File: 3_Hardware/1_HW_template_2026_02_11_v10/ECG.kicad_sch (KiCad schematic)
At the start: 25 parts, among them U5 AD8232ACPZ-R7

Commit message: added datasheet and started layout
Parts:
- renumbered LA to LA1, RA to RA1, RL to RL1
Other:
- moved on the sheet: C25, C26, C27, C28, C29, C30, C31, LA1, R23, R24, R25, R28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

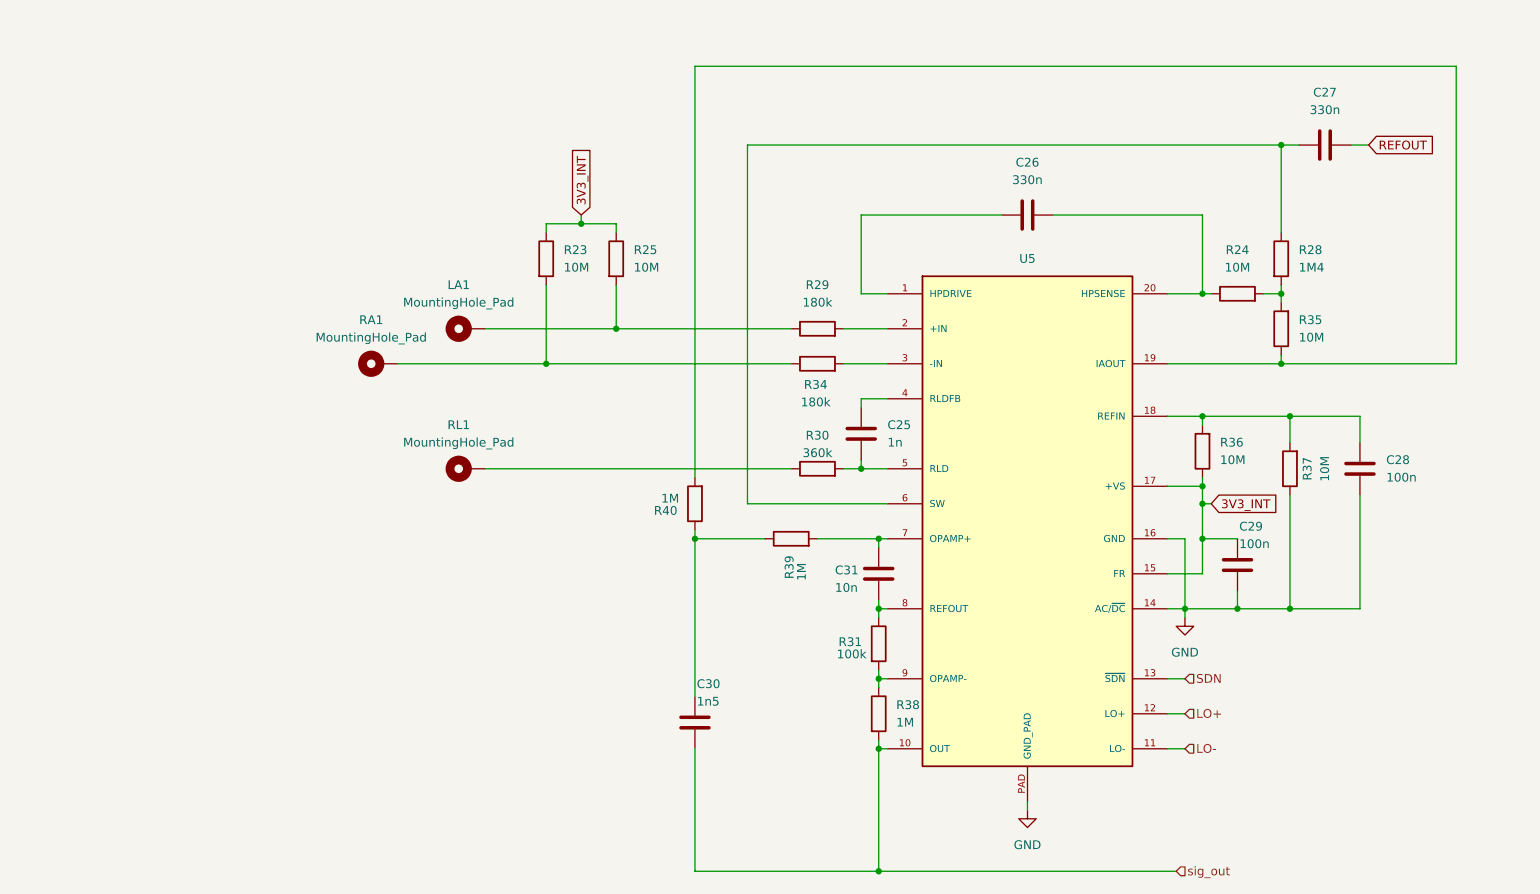
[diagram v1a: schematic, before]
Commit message: updated layout
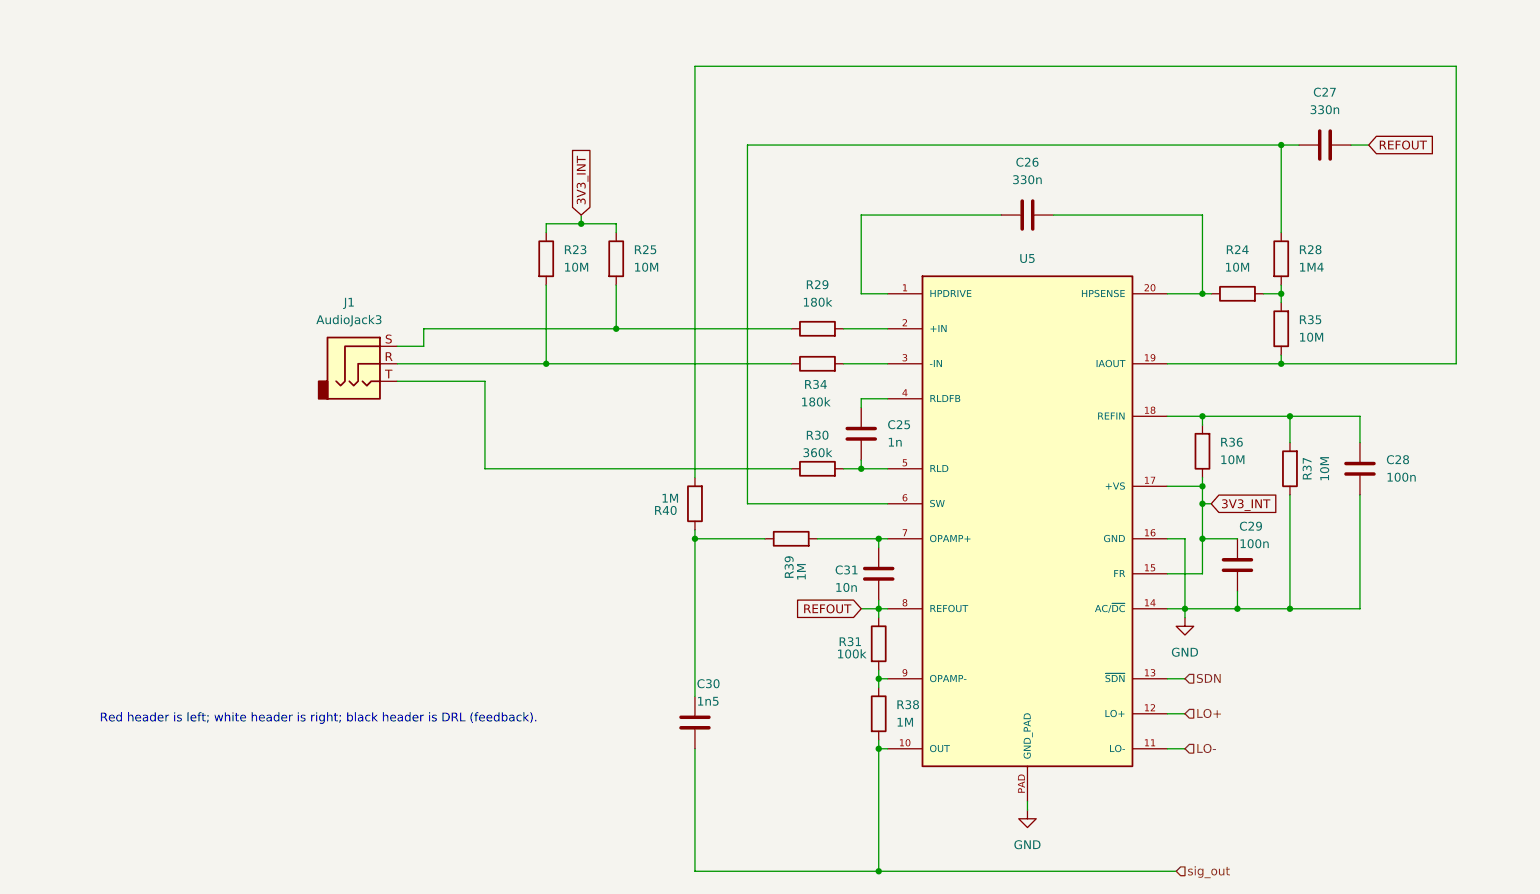
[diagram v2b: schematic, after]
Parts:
- removed LA1, RA1, RL1: MountingHole_Pad, TestPoint:TestPoint_Loop_D2.60mm_Drill1.6mm_Beaded, symbol Mechanical:MountingHole_Pad
- added J1: AudioJack3, Connector_Audio:Jack_3.5mm_CUI_SJ-3523-SMT_Horizontal, symbol Connector_Audio:AudioJack3
- R23, R24, R25, R28, R29, R30, R31, R34, R35, R36, R37, R38, R39, R40: footprint Resistor_SMD:R_0805_2012Metric_Pad1.20x1.40mm_HandSolder -> Resistor_SMD:R_0603_1608Metric_Pad0.98x0.95mm_HandSolder
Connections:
- net REFOUT: now also C31.1, R31.1, U5.8 (REFOUT)
- net at R23.2, R34.1: now also J1.R
- net at R25.2, R29.1: now also J1.S
- net at R30.1: now also J1.T
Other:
- note added: "Red header is left; white header is right; black header is DRL (feedback)."

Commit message: updated layout
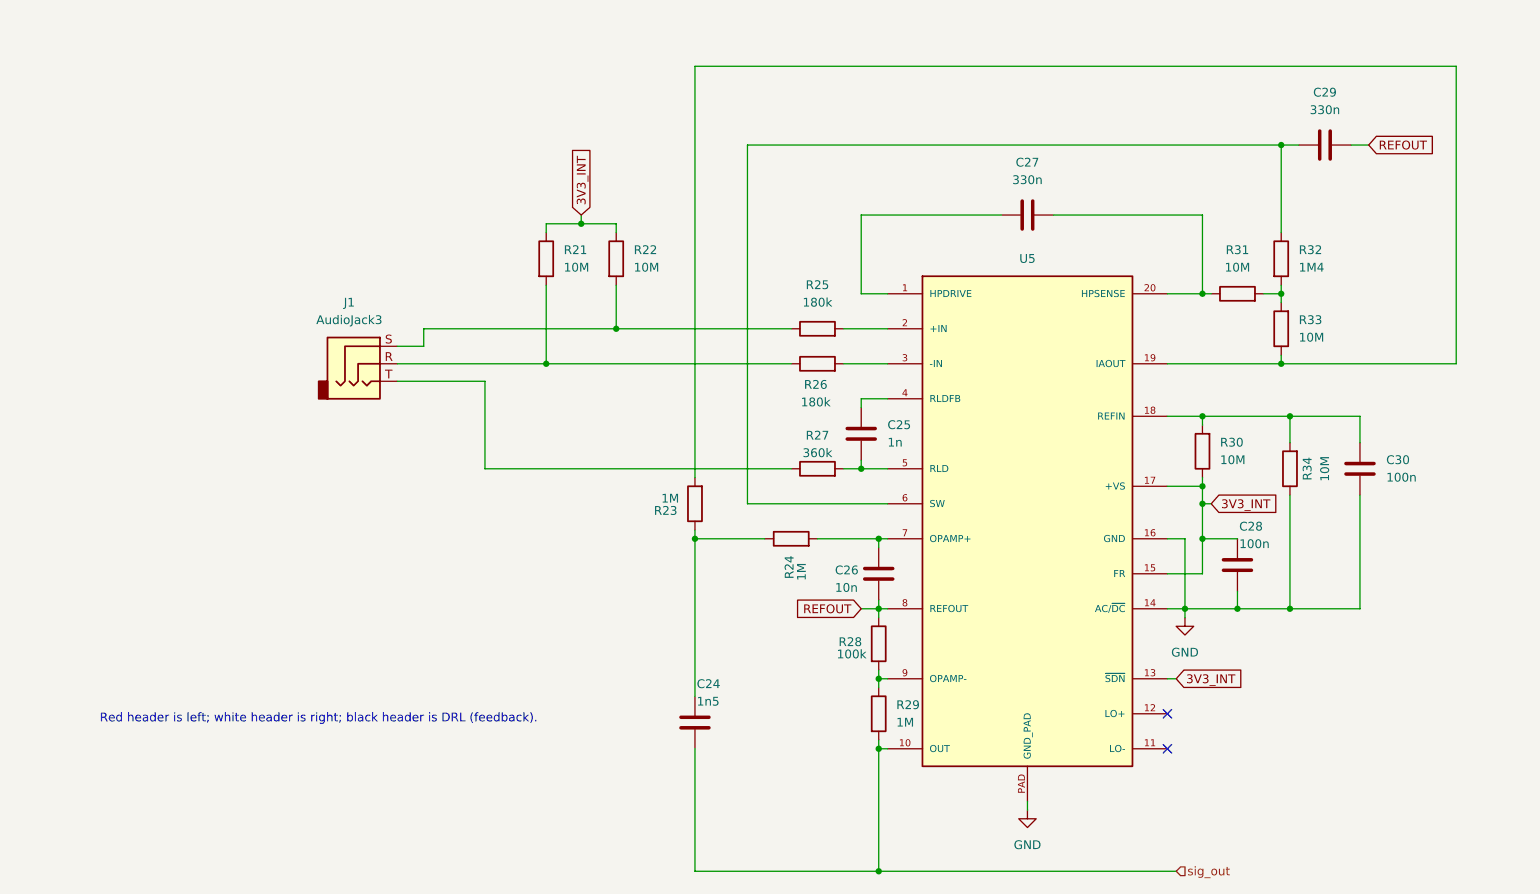
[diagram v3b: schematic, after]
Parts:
- renumbered C30 to C24, C31 to C26, C26 to C27, C29 to C28, C27 to C29, C28 to C30, R23 to R21, R25 to R22, R40 to R23, R39 to R24, R29 to R25, R34 to R26, R30 to R27, R31 to R28, R38 to R29, R36 to R30, R24 to R31, R28 to R32, R35 to R33, R37 to R34
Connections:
- net SDN is gone; now on net 3V3_INT: U5.13 (~{SDN})
- net LO+: no longer names the net of U5.12 (LO+)
- net LO-: no longer names the net of U5.11 (LO-)
- no-connect marks 0 -> 2
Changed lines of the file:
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@@
 		(color 0 0 0 0)
 	)
+	(no_connect
+		(at 175.26 128.27)
+	)
+	(no_connect
+		(at 175.26 123.19)
+	)
 	(wire
 		(pts
@@
 	(wire
 		(pts
+			(xy 176.53 118.11) (xy 175.26 118.11)
+		)
+		(stroke
+			(width 0)
+			(type default)
+		)
+	)
+	(wire
+		(pts
 			(xy 133.35 97.79) (xy 134.62 97.79)
 		)
@@
 	(wire
 		(pts
-			(xy 175.26 123.19) (xy 177.8 123.19)
-		)
-		(stroke
-			(width 0)
-			(type default)
-		)
-	)
-	(wire
-		(pts
 			(xy 193.04 80.01) (xy 193.04 83.82)
 		)
@@
 	(wire
 		(pts
-			(xy 175.26 128.27) (xy 177.8 128.27)
-		)
-		(stroke
-			(width 0)
-			(type default)
-		)
-	)
-	(wire
-		(pts
 			(xy 180.34 50.8) (xy 180.34 62.23)
 		)
@@
 	(wire
 		(pts
-			(xy 175.26 118.11) (xy 177.8 118.11)
-		)
-		(stroke
-			(width 0)
-			(type default)
-		)
-	)
-	(wire
-		(pts
 			(xy 106.68 96.52) (xy 106.68 97.79)
 		)
@@
 		)
 	)
-	(global_label "REFOUT"
+	(global_label "3V3_INT"
 		(shape input)
-		(at 130.81 107.95 180)
+		(at 176.53 118.11 0)
 		(fields_autoplaced yes)
 		(effects
@@
 				(size 1.27 1.27)
 			)
-			(justify right)
+			(justify left)
 		)
 		(property "Intersheetrefs" "${INTERSHEET_REFS}"
-			(at 120.6886 107.95 0)
+			(at 186.8933 118.11 0)
 			(effects
 				(font
 					(size 1.27 1.27)
 				)
-				(justify right)
+				(justify left)
 				(hide yes)
 			)
 		)
 	)
-	(hierarchical_label "LO-"
-		(shape input)
-		(at 177.8 128.27 0)
-		(effects
-			(font
-				(size 1.27 1.27)
-			)
-			(justify left)
-		)
-	)
-	(hierarchical_label "sig_out"
+	(global_label "REFOUT"
 		(shape input)
-		(at 176.53 146.05 0)
+		(at 130.81 107.95 180)
+		(fields_autoplaced yes)
 		(effects
 			(font
 				(size 1.27 1.27)
 			)
-			(justify left)
+			(justify right)
 		)
-	)
-	(hierarchical_label "LO+"
-		(shape input)
-		(at 177.8 123.19 0)
-		(effects
-			(font
-				(size 1.27 1.27)
+		(property "Intersheetrefs" "${INTERSHEET_REFS}"
+			(at 120.6886 107.95 0)
+			(effects
+				(font
+					(size 1.27 1.27)
+				)
+				(justify right)
+				(hide yes)
 			)
-			(justify left)
 		)
 	)
-	(hierarchical_label "SDN"
+	(hierarchical_label "sig_out"
 		(shape input)
-		(at 177.8 118.11 0)
+		(at 176.53 146.05 0)
 		(effects
 			(font
@@
 		(on_board yes)
 		(dnp no)
-		(property "Reference" "R34"
+		(property "Reference" "R26"
 			(at 124.206 75.438 90)
 			(effects
@@
 			(project "HW_template"
 				(path "/1f276d59-ad9b-4e70-a842-f3b7e562eb9b/0fb14f5e-532a-4fc6-a21e-2193a42ea5a4"
-					(reference "R34")
+					(reference "R26")
 					(unit 1)
 				)
@@
 		(dnp no)
 		(fields_autoplaced yes)
-		(property "Reference" "R36"
+		(property "Reference" "R30"
 			(at 182.88 83.8199 0)
 			(effects
@@
 			(project "HW_template"
 				(path "/1f276d59-ad9b-4e70-a842-f3b7e562eb9b/0fb14f5e-532a-4fc6-a21e-2193a42ea5a4"
-					(reference "R36")
+					(reference "R30")
 					(unit 1)
 				)
@@
 		(dnp no)
 		(fields_autoplaced yes)
-		(property "Reference" "#PWR041"
+		(property "Reference" "#PWR040"
 			(at 177.8 115.57 0)
 			(effects
@@
 			(project "HW_template"
 				(path "/1f276d59-ad9b-4e70-a842-f3b7e562eb9b/0fb14f5e-532a-4fc6-a21e-2193a42ea5a4"
-					(reference "#PWR041")
+					(reference "#PWR040")
 					(unit 1)
 				)
@@
 		(dnp no)
 		(fields_autoplaced yes)
-		(property "Reference" "R35"
+		(property "Reference" "R33"
 			(at 194.31 66.0399 0)
 			(effects
@@
 			(project "HW_template"
 				(path "/1f276d59-ad9b-4e70-a842-f3b7e562eb9b/0fb14f5e-532a-4fc6-a21e-2193a42ea5a4"
-					(reference "R35")
+					(reference "R33")
 					(unit 1)
 				)
@@
 		(on_board yes)
 		(dnp no)
-		(property "Reference" "R40"
+		(property "Reference" "R23"
 			(at 104.14 93.726 0)
 			(effects
@@
 			(project "HW_template"
 				(path "/1f276d59-ad9b-4e70-a842-f3b7e562eb9b/0fb14f5e-532a-4fc6-a21e-2193a42ea5a4"
-					(reference "R40")
+					(reference "R23")
 					(unit 1)
 				)
@@
 		(on_board yes)
 		(dnp no)
-		(property "Reference" "C30"
+		(property "Reference" "C24"
 			(at 106.934 118.872 0)
 			(effects
@@
 			(project "HW_template"
 				(path "/1f276d59-ad9b-4e70-a842-f3b7e562eb9b/0fb14f5e-532a-4fc6-a21e-2193a42ea5a4"
-					(reference "C30")
+					(reference "C24")
 					(unit 1)
 				)
@@
 		(dnp no)
 		(fields_autoplaced yes)
-		(property "Reference" "#PWR040"
+		(property "Reference" "#PWR039"
 			(at 154.94 143.51 0)
 			(effects
@@
 			(project "HW_template"
 				(path "/1f276d59-ad9b-4e70-a842-f3b7e562eb9b/0fb14f5e-532a-4fc6-a21e-2193a42ea5a4"
-					(reference "#PWR040")
+					(reference "#PWR039")
 					(unit 1)
 				)
@@
 		(dnp no)
 		(fields_autoplaced yes)
-		(property "Reference" "C26"
+		(property "Reference" "C27"
 			(at 154.94 43.18 90)
 			(effects
@@
 			(project "HW_template"
 				(path "/1f276d59-ad9b-4e70-a842-f3b7e562eb9b/0fb14f5e-532a-4fc6-a21e-2193a42ea5a4"
-					(reference "C26")
+					(reference "C27")
 					(unit 1)
 				)
@@
 		(on_board yes)
 		(dnp no)
-		(property "Reference" "C29"
+		(property "Reference" "C28"
 			(at 185.674 96.012 0)
 			(effects
@@
 			(project "HW_template"
 				(path "/1f276d59-ad9b-4e70-a842-f3b7e562eb9b/0fb14f5e-532a-4fc6-a21e-2193a42ea5a4"
-					(reference "C29")
+					(reference "C28")
 					(unit 1)
 				)
@@
 		(dnp no)
 		(fields_autoplaced yes)
-		(property "Reference" "C27"
+		(property "Reference" "C29"
 			(at 198.12 33.02 90)
 			(effects
@@
 			(project "HW_template"
 				(path "/1f276d59-ad9b-4e70-a842-f3b7e562eb9b/0fb14f5e-532a-4fc6-a21e-2193a42ea5a4"
-					(reference "C27")
+					(reference "C29")
 					(unit 1)
 				)
@@
 		(on_board yes)
 		(dnp no)
-		(property "Reference" "R37"
+		(property "Reference" "R34"
 			(at 195.58 87.63 90)
 			(effects
@@
 			(project "HW_template"
 				(path "/1f276d59-ad9b-4e70-a842-f3b7e562eb9b/0fb14f5e-532a-4fc6-a21e-2193a42ea5a4"
-					(reference "R37")
+					(reference "R34")
 					(unit 1)
 				)
@@
 		(dnp no)
 		(fields_autoplaced yes)
-		(property "Reference" "R38"
+		(property "Reference" "R29"
 			(at 135.89 121.9199 0)
 			(effects
@@
 			(project "HW_template"
 				(path "/1f276d59-ad9b-4e70-a842-f3b7e562eb9b/0fb14f5e-532a-4fc6-a21e-2193a42ea5a4"
-					(reference "R38")
+					(reference "R29")
 					(unit 1)
 				)
@@
 		(dnp no)
 		(fields_autoplaced yes)
-		(property "Reference" "R28"
+		(property "Reference" "R32"
 			(at 194.31 55.8799 0)
 			(effects
@@
 			(project "HW_template"
 				(path "/1f276d59-ad9b-4e70-a842-f3b7e562eb9b/0fb14f5e-532a-4fc6-a21e-2193a42ea5a4"
-					(reference "R28")
+					(reference "R32")
 					(unit 1)
 				)
@@
 		(dnp no)
 		(fields_autoplaced yes)
-		(property "Reference" "C28"
+		(property "Reference" "C30"
 			(at 207.01 86.3599 0)
 			(effects
@@
 			(project "HW_template"
 				(path "/1f276d59-ad9b-4e70-a842-f3b7e562eb9b/0fb14f5e-532a-4fc6-a21e-2193a42ea5a4"
-					(reference "C28")
+					(reference "C30")
 					(unit 1)
 				)
@@
 		(dnp no)
 		(fields_autoplaced yes)
-		(property "Reference" "R29"
+		(property "Reference" "R25"
 			(at 124.46 60.96 90)
 			(effects
@@
 			(project "HW_template"
 				(path "/1f276d59-ad9b-4e70-a842-f3b7e562eb9b/0fb14f5e-532a-4fc6-a21e-2193a42ea5a4"
-					(reference "R29")
+					(reference "R25")
 					(unit 1)
 				)
@@
 		(on_board yes)
 		(dnp no)
-		(property "Reference" "C31"
+		(property "Reference" "C26"
 			(at 127 102.362 0)
 			(effects
@@
 			(project "HW_template"
 				(path "/1f276d59-ad9b-4e70-a842-f3b7e562eb9b/0fb14f5e-532a-4fc6-a21e-2193a42ea5a4"
-					(reference "C31")
+					(reference "C26")
 					(unit 1)
 				)
@@
 		(dnp no)
 		(fields_autoplaced yes)
-		(property "Reference" "R23"
+		(property "Reference" "R21"
 			(at 87.63 55.8799 0)
 			(effects
@@
 			(project "HW_template"
 				(path "/1f276d59-ad9b-4e70-a842-f3b7e562eb9b/0fb14f5e-532a-4fc6-a21e-2193a42ea5a4"
-					(reference "R23")
+					(reference "R21")
 					(unit 1)
 				)
@@
 		(dnp no)
 		(fields_autoplaced yes)
-		(property "Reference" "R24"
+		(property "Reference" "R31"
 			(at 185.42 55.88 90)
 			(effects
@@
 			(project "HW_template"
 				(path "/1f276d59-ad9b-4e70-a842-f3b7e562eb9b/0fb14f5e-532a-4fc6-a21e-2193a42ea5a4"
-					(reference "R24")
+					(reference "R31")
 					(unit 1)
 				)
@@
 		(on_board yes)
 		(dnp no)
-		(property "Reference" "R39"
+		(property "Reference" "R24"
 			(at 120.396 103.632 0)
 			(effects
@@
 			(project "HW_template"
 				(path "/1f276d59-ad9b-4e70-a842-f3b7e562eb9b/0fb14f5e-532a-4fc6-a21e-2193a42ea5a4"
-					(reference "R39")
+					(reference "R24")
 					(unit 1)
 				)
@@
 		(on_board yes)
 		(dnp no)
-		(property "Reference" "R31"
+		(property "Reference" "R28"
 			(at 127.508 112.776 0)
 			(effects
@@
 			(project "HW_template"
 				(path "/1f276d59-ad9b-4e70-a842-f3b7e562eb9b/0fb14f5e-532a-4fc6-a21e-2193a42ea5a4"
-					(reference "R31")
+					(reference "R28")
 					(unit 1)
 				)
@@
 		(on_board yes)
 		(dnp no)
-		(property "Reference" "R30"
+		(property "Reference" "R27"
 			(at 124.46 82.804 90)
 			(effects
@@
 			(project "HW_template"
 				(path "/1f276d59-ad9b-4e70-a842-f3b7e562eb9b/0fb14f5e-532a-4fc6-a21e-2193a42ea5a4"
-					(reference "R30")
+					(reference "R27")
 					(unit 1)
 				)
@@
 		(dnp no)
 		(fields_autoplaced yes)
-		(property "Reference" "R25"
+		(property "Reference" "R22"
 			(at 97.79 55.8799 0)
 			(effects
@@
 			(project "HW_template"
 				(path "/1f276d59-ad9b-4e70-a842-f3b7e562eb9b/0fb14f5e-532a-4fc6-a21e-2193a42ea5a4"
-					(reference "R25")
+					(reference "R22")
 					(unit 1)
 				)

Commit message: pcb schematics finished + layout
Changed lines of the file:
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@@
 	)
 	(hierarchical_label "sig_out"
-		(shape input)
+		(shape output)
 		(at 176.53 146.05 0)
 		(effects
@@
 			)
 		)
-		(property "Datasheet" ""
+		(property "Datasheet" "https://www.analog.com/media/en/technical-documentation/data-sheets/ad8232.pdf"
 			(at 154.94 102.87 0)
 			(effects
